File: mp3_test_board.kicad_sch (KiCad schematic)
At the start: 0 parts

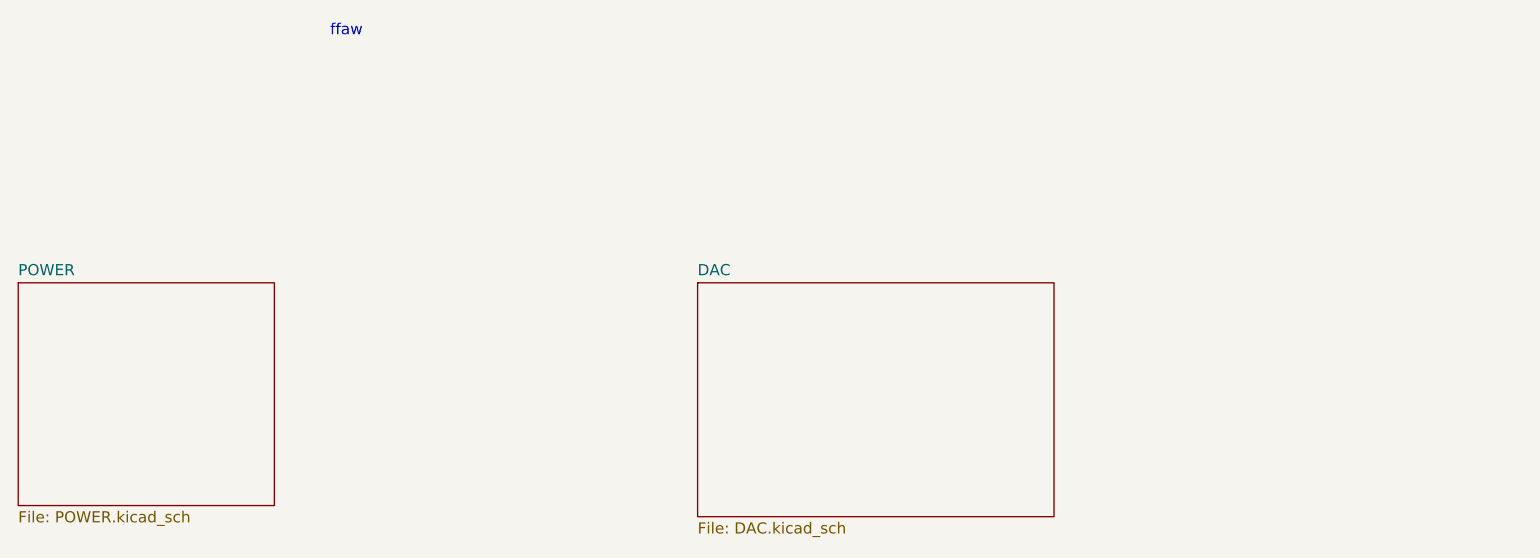
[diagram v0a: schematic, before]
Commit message: added SOC list
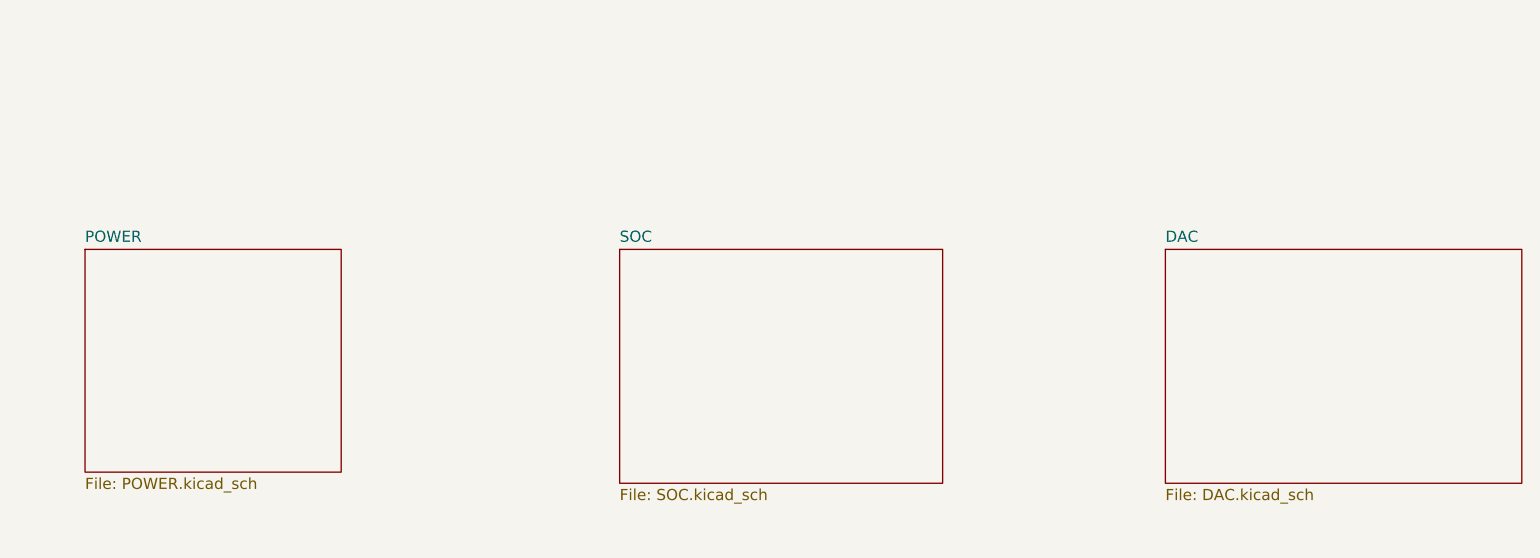
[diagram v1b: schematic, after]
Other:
- added sheet SOC (SOC.kicad_sch)
- note removed: "ffaw"
